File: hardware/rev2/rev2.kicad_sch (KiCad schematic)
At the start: 2 parts, among them J1 Conn_Coaxial_Small

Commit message: did some schematic stuff
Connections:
- net SX1262/Antenna: now reaches J1.1 (In)
- net GND: now reaches J1.2 (Ext)
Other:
- sheet SX1262 ports: added Antenna, BUSY, CS, DIO1, MISO, MOSI, Reset, SCK; removed none
- note added: "Cursed ribbonkabelantenn"
- moved on the sheet: J1

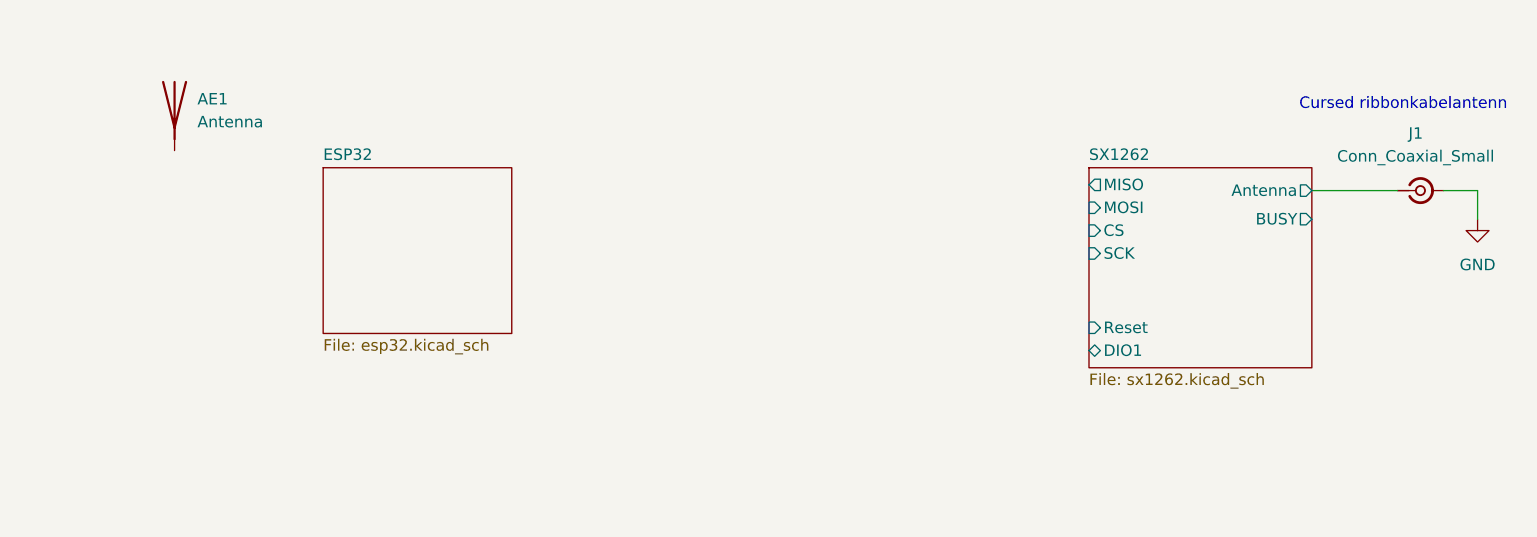
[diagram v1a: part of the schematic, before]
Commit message: wired SPI pins for SX1262
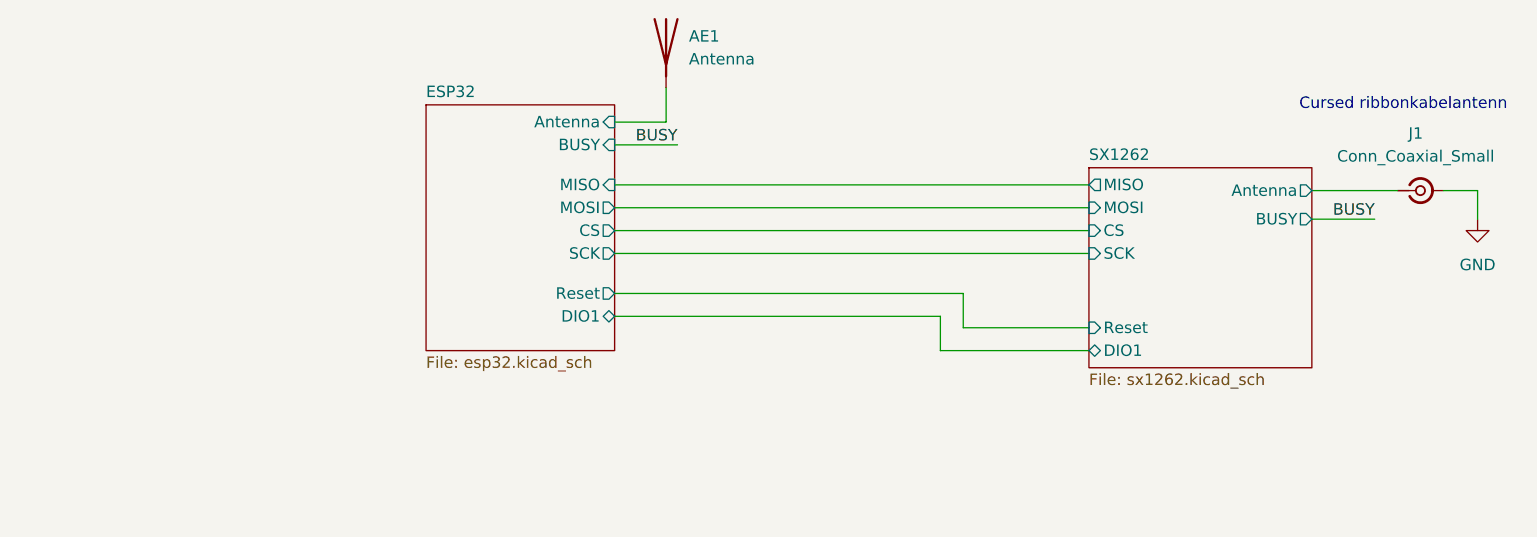
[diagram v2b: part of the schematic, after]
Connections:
- net ESP32/Antenna: now reaches AE1.1 (A)
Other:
- sheet ESP32 ports: added Antenna, BUSY, CS, DIO1, MISO, MOSI, Reset, SCK; removed none
- moved on the sheet: AE1
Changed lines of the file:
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@@
+	(wire
+		(pts
+			(xy 153.67 79.375) (xy 137.16 79.375)
+		)
+		(stroke
+			(width 0)
+			(type default)
+		)
+	)
+	(wire
+		(pts
+			(xy 100.965 68.58) (xy 153.67 68.58)
+		)
+		(stroke
+			(width 0)
+			(type default)
+		)
+	)
+	(wire
+		(pts
+			(xy 139.7 73.025) (xy 139.7 76.835)
+		)
+		(stroke
+			(width 0)
+			(type default)
+		)
+	)
+	(wire
+		(pts
+			(xy 100.965 60.96) (xy 153.67 60.96)
+		)
+		(stroke
+			(width 0)
+			(type default)
+		)
+	)
+	(wire
+		(pts
+			(xy 106.68 53.975) (xy 106.68 50.165)
+		)
+		(stroke
+			(width 0)
+			(type default)
+		)
+	)
 	(wire
 		(pts
@@
 	(wire
 		(pts
+			(xy 137.16 75.565) (xy 100.965 75.565)
+		)
+		(stroke
+			(width 0)
+			(type default)
+		)
+	)
+	(wire
+		(pts
 			(xy 178.435 61.595) (xy 187.96 61.595)
 		)
@@
 	(wire
 		(pts
+			(xy 100.965 63.5) (xy 153.67 63.5)
+		)
+		(stroke
+			(width 0)
+			(type default)
+		)
+	)
+	(wire
+		(pts
+			(xy 100.965 53.975) (xy 106.68 53.975)
+		)
+		(stroke
+			(width 0)
+			(type default)
+		)
+	)
+	(wire
+		(pts
+			(xy 185.42 64.77) (xy 178.435 64.77)
+		)
+		(stroke
+			(width 0)
+			(type default)
+		)
+	)
+	(wire
+		(pts
+			(xy 100.965 73.025) (xy 139.7 73.025)
+		)
+		(stroke
+			(width 0)
+			(type default)
+		)
+	)
+	(wire
+		(pts
 			(xy 196.85 64.77) (xy 196.85 61.595)
 		)
@@
 			(width 0)
 			(type default)
+		)
+	)
+	(wire
+		(pts
+			(xy 100.965 66.04) (xy 153.67 66.04)
+		)
+		(stroke
+			(width 0)
+			(type default)
+		)
+	)
+	(wire
+		(pts
+			(xy 137.16 79.375) (xy 137.16 75.565)
+		)
+		(stroke
+			(width 0)
+			(type default)
+		)
+	)
+	(wire
+		(pts
+			(xy 139.7 76.835) (xy 153.67 76.835)
+		)
+		(stroke
+			(width 0)
+			(type default)
+		)
+	)
+	(wire
+		(pts
+			(xy 107.95 56.515) (xy 100.965 56.515)
+		)
+		(stroke
+			(width 0)
+			(type default)
+		)
+	)
+	(label "BUSY"
+		(at 185.42 64.77 180)
+		(effects
+			(font
+				(size 1.27 1.27)
+			)
+			(justify right bottom)
+		)
+	)
+	(label "BUSY"
+		(at 107.95 56.515 180)
+		(effects
+			(font
+				(size 1.27 1.27)
+			)
+			(justify right bottom)
 		)
 	)
 	(symbol
 		(lib_id "Device:Antenna")
-		(at 52.07 52.07 0)
+		(at 106.68 45.085 0)
 		(unit 1)
 		(body_style 1)
@@
 		(fields_autoplaced yes)
 		(property "Reference" "AE1"
-			(at 54.61 51.4349 0)
+			(at 109.22 44.4499 0)
 			(show_name no)
 			(do_not_autoplace no)
@@
 		)
 		(property "Value" "Antenna"
-			(at 54.61 53.9749 0)
+			(at 109.22 46.9899 0)
 			(show_name no)
 			(do_not_autoplace no)
@@
 		)
 		(property "Footprint" ""
-			(at 52.07 52.07 0)
+			(at 106.68 45.085 0)
 			(hide yes)
 			(show_name no)
@@
 		)
 		(property "Datasheet" ""
-			(at 52.07 52.07 0)
+			(at 106.68 45.085 0)
 			(hide yes)
 			(show_name no)
@@
 		)
 		(property "Description" "Antenna"
-			(at 52.07 52.07 0)
+			(at 106.68 45.085 0)
 			(hide yes)
 			(show_name no)
@@
 	)
 	(sheet
-		(at 68.58 59.055)
-		(size 20.955 18.415)
+		(at 80.01 52.07)
+		(size 20.955 27.305)
 		(exclude_from_sim no)
 		(in_bom yes)
@@
 		)
 		(property "Sheetname" "ESP32"
-			(at 68.58 58.3434 0)
+			(at 80.01 51.3584 0)
 			(show_name no)
 			(do_not_autoplace no)
@@
 		)
 		(property "Sheetfile" "esp32.kicad_sch"
-			(at 68.58 78.0546 0)
+			(at 80.01 79.9596 0)
 			(show_name no)
 			(do_not_autoplace no)
@@
 			)
 		)
+		(pin "Antenna" input
+			(at 100.965 53.975 0)
+			(effects
+				(font
+					(size 1.27 1.27)
+				)
+				(justify right)
+			)
+		)
+		(pin "BUSY" input
+			(at 100.965 56.515 0)
+			(effects
+				(font
+					(size 1.27 1.27)
+				)
+				(justify right)
+			)
+		)
+		(pin "CS" output
+			(at 100.965 66.04 0)
+			(effects
+				(font
+					(size 1.27 1.27)
+				)
+				(justify right)
+			)
+		)
+		(pin "DIO1" bidirectional
+			(at 100.965 75.565 0)
+			(effects
+				(font
+					(size 1.27 1.27)
+				)
+				(justify right)
+			)
+		)
+		(pin "MISO" input
+			(at 100.965 60.96 0)
+			(effects
+				(font
+					(size 1.27 1.27)
+				)
+				(justify right)
+			)
+		)
+		(pin "MOSI" output
+			(at 100.965 63.5 0)
+			(effects
+				(font
+					(size 1.27 1.27)
+				)
+				(justify right)
+			)
+		)
+		(pin "Reset" output
+			(at 100.965 73.025 0)
+			(effects
+				(font
+					(size 1.27 1.27)
+				)
+				(justify right)
+			)
+		)
+		(pin "SCK" output
+			(at 100.965 68.58 0)
+			(effects
+				(font
+					(size 1.27 1.27)
+				)
+				(justify right)
+			)
+		)

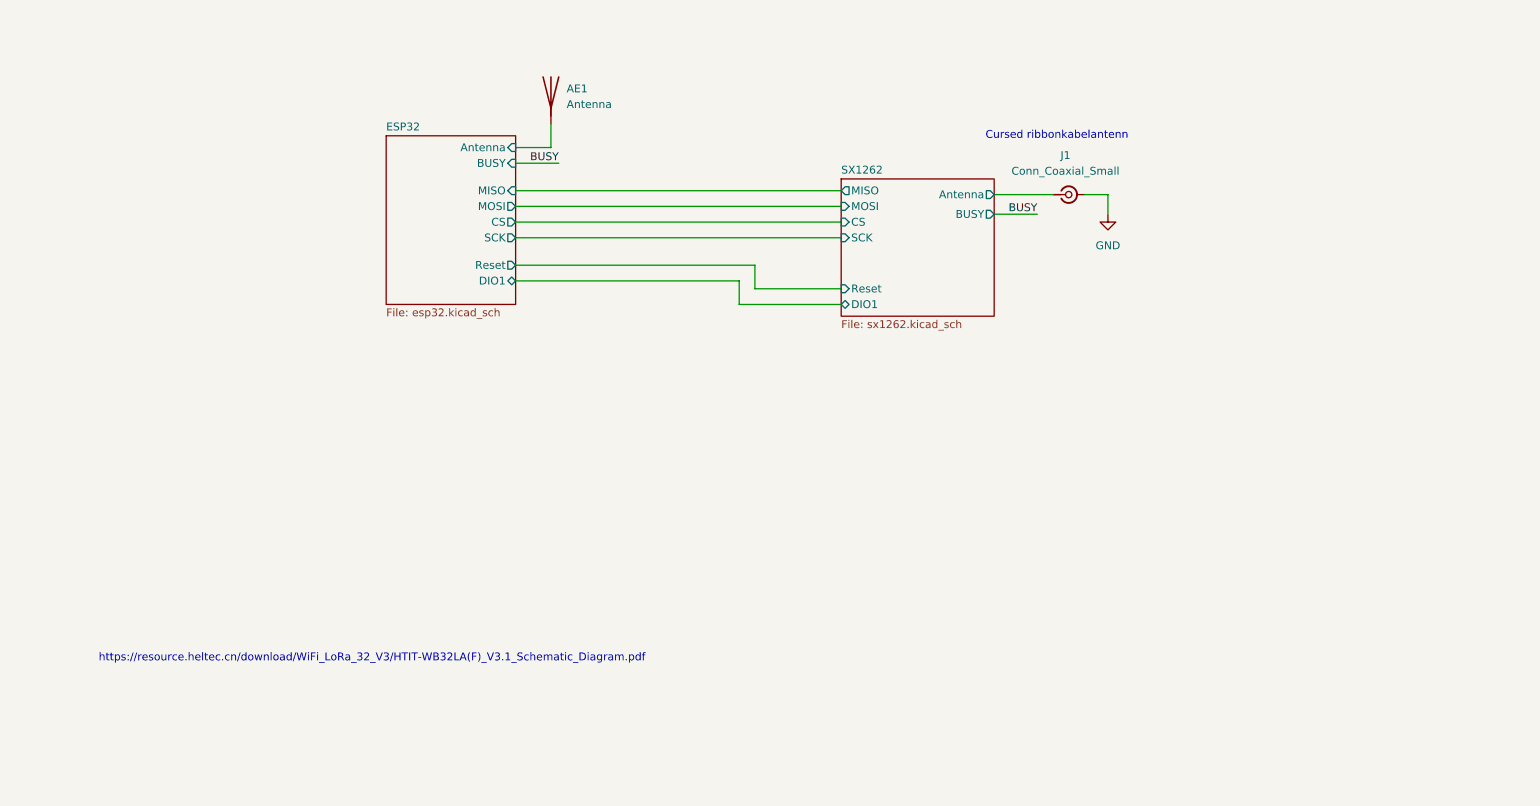
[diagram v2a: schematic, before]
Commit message: cleaned up esp32 and added antenna stuff on main sheet
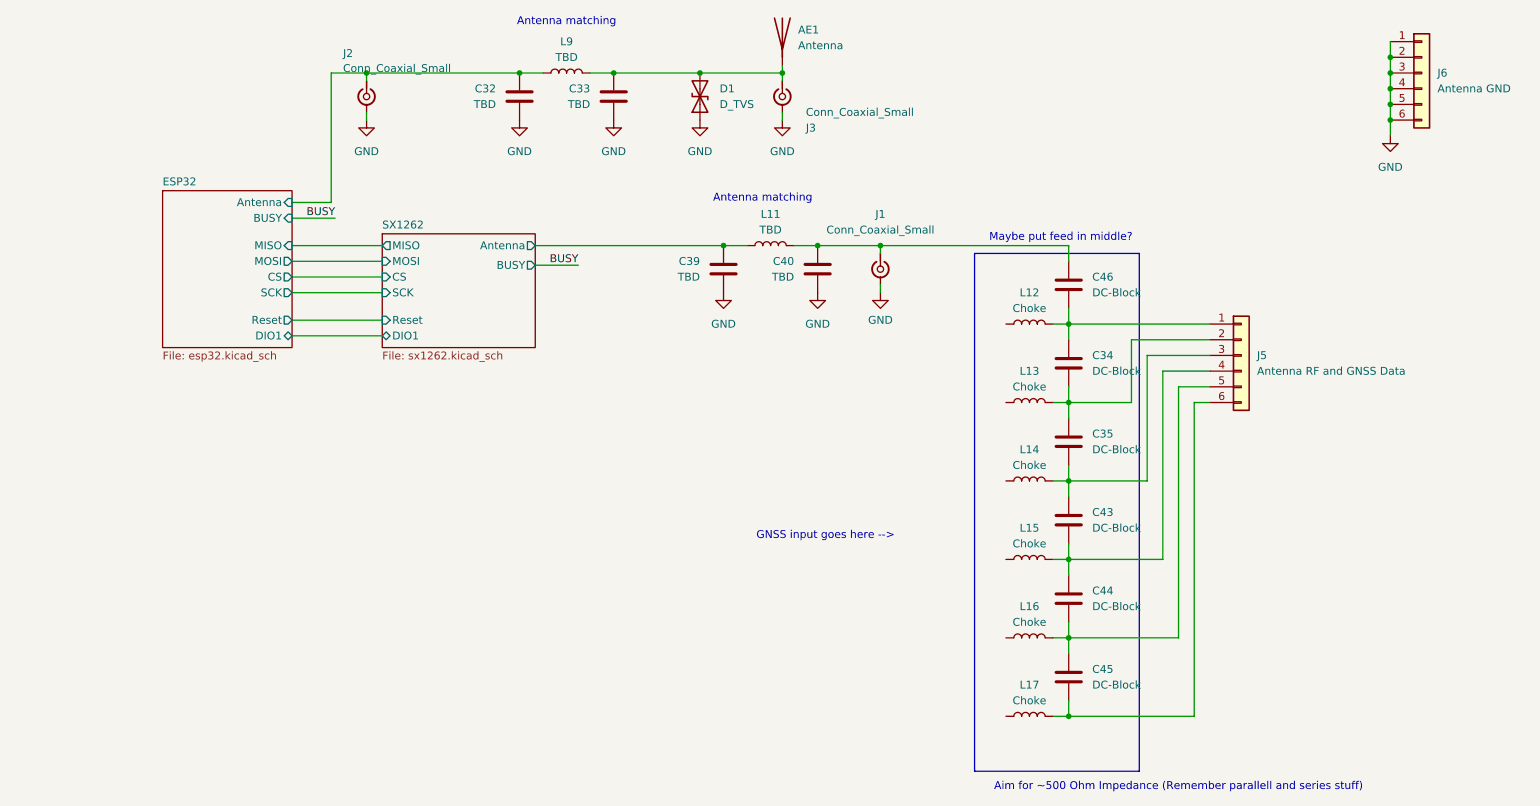
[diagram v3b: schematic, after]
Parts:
- added C32, C33, C39, C40: TBD, symbol Device:C
- added C34, C35, C43, C44, C45, C46: DC-Block, symbol Device:C
- added D1: D_TVS, symbol Device:D_TVS
- added J2, J3: Conn_Coaxial_Small, symbol Connector:Conn_Coaxial_Small
- added J5: Antenna RF and GNSS Data, symbol Connector_Generic:Conn_01x06
- added J6: Antenna GND, symbol Connector_Generic:Conn_01x06
- added L11, L9: TBD, symbol Device:L
- added L12, L13, L14, L15, L16, L17: Choke, symbol Device:L
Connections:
- net ESP32/Antenna: now also C32.1, J2.1 (In), L9.2; no longer AE1.1 (A)
- net GND: now also C32.2, C33.2, C39.2, C40.2, D1.1 (A1), J2.2 (Ext), J3.2 (Ext), J6.1 (Pin_1), J6.2 (Pin_2), J6.3 (Pin_3), J6.4 (Pin_4), J6.5 (Pin_5), J6.6 (Pin_6)
- net SX1262/Antenna: now also C39.1, L11.2; no longer J1.1 (In)
- new net: C34.2, C35.1, J5.2 (Pin_2), L13.2
- new net: C35.2, C43.1, J5.3 (Pin_3), L14.2
- new net: C43.2, C44.1, J5.4 (Pin_4), L15.2
- new net: C44.2, C45.1, J5.5 (Pin_5), L16.2
- new net: AE1.1 (A), C33.1, D1.2 (A2), J3.1 (In), L9.1
- new net: C34.1, C46.2, J5.1 (Pin_1), L12.2
- new net: C45.2, J5.6 (Pin_6), L17.2
- new net: C40.1, C46.1, J1.1 (In), L11.1
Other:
- note added: "Aim for ~500 Ohm Impedance (Remember parallell and series stuff)"
- note added: "Antenna matching"
- note added: "GNSS input goes here -->"
- note added: "Maybe put feed in middle?"
- note removed: "Cursed ribbonkabelantenn"
- note removed: "https://resource.heltec.cn/download/WiFi_LoRa_32_V3/HTIT-WB32LA(F)_V3.1_Schematic_Diagram.pdf"

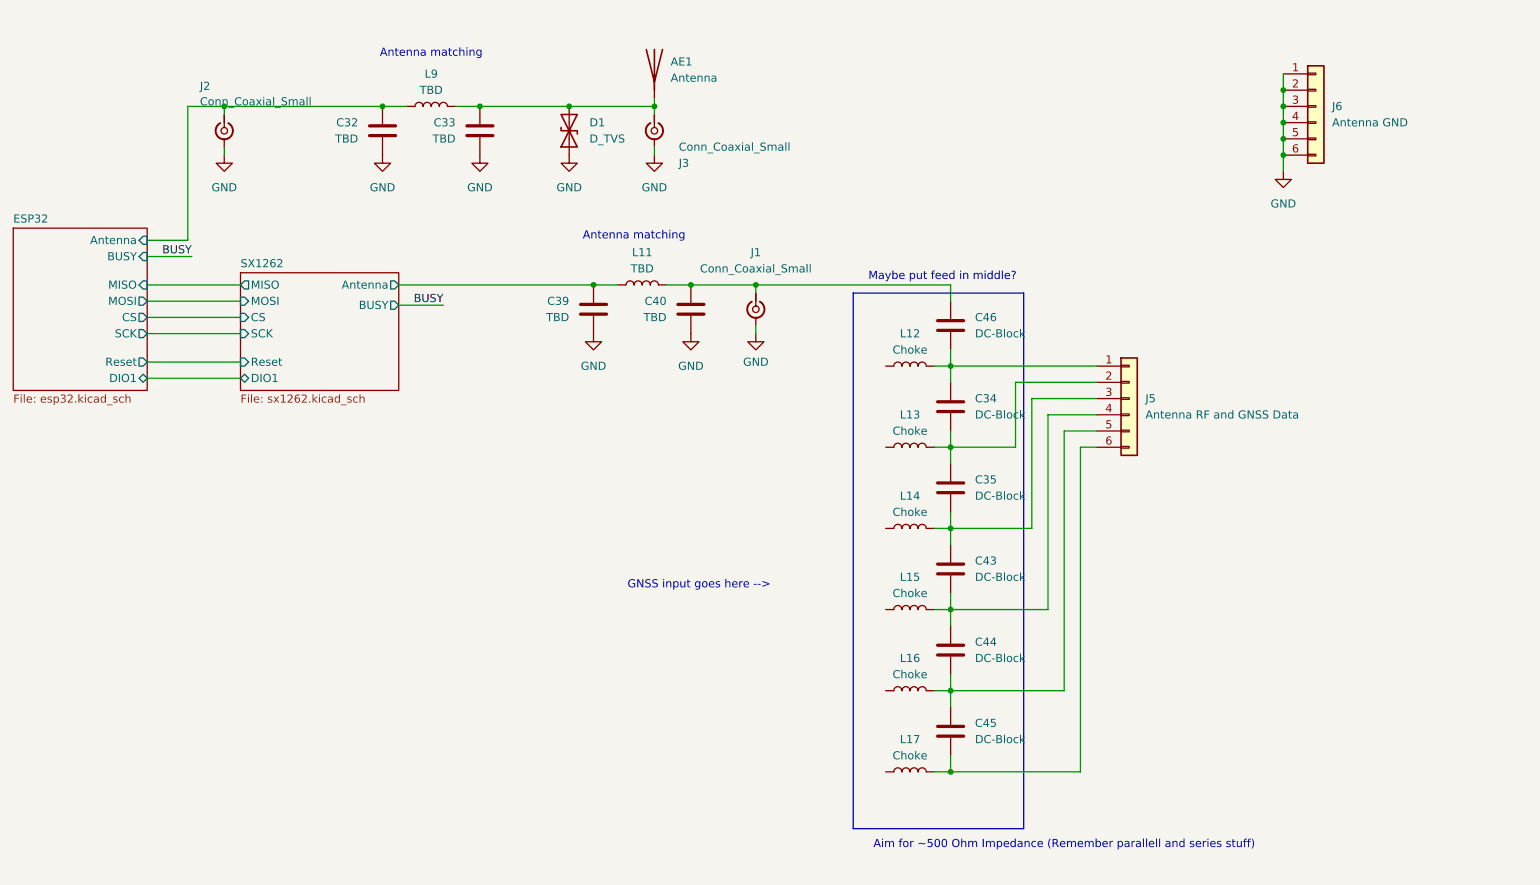
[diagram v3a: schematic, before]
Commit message: added power, net classes and some antenna stuff
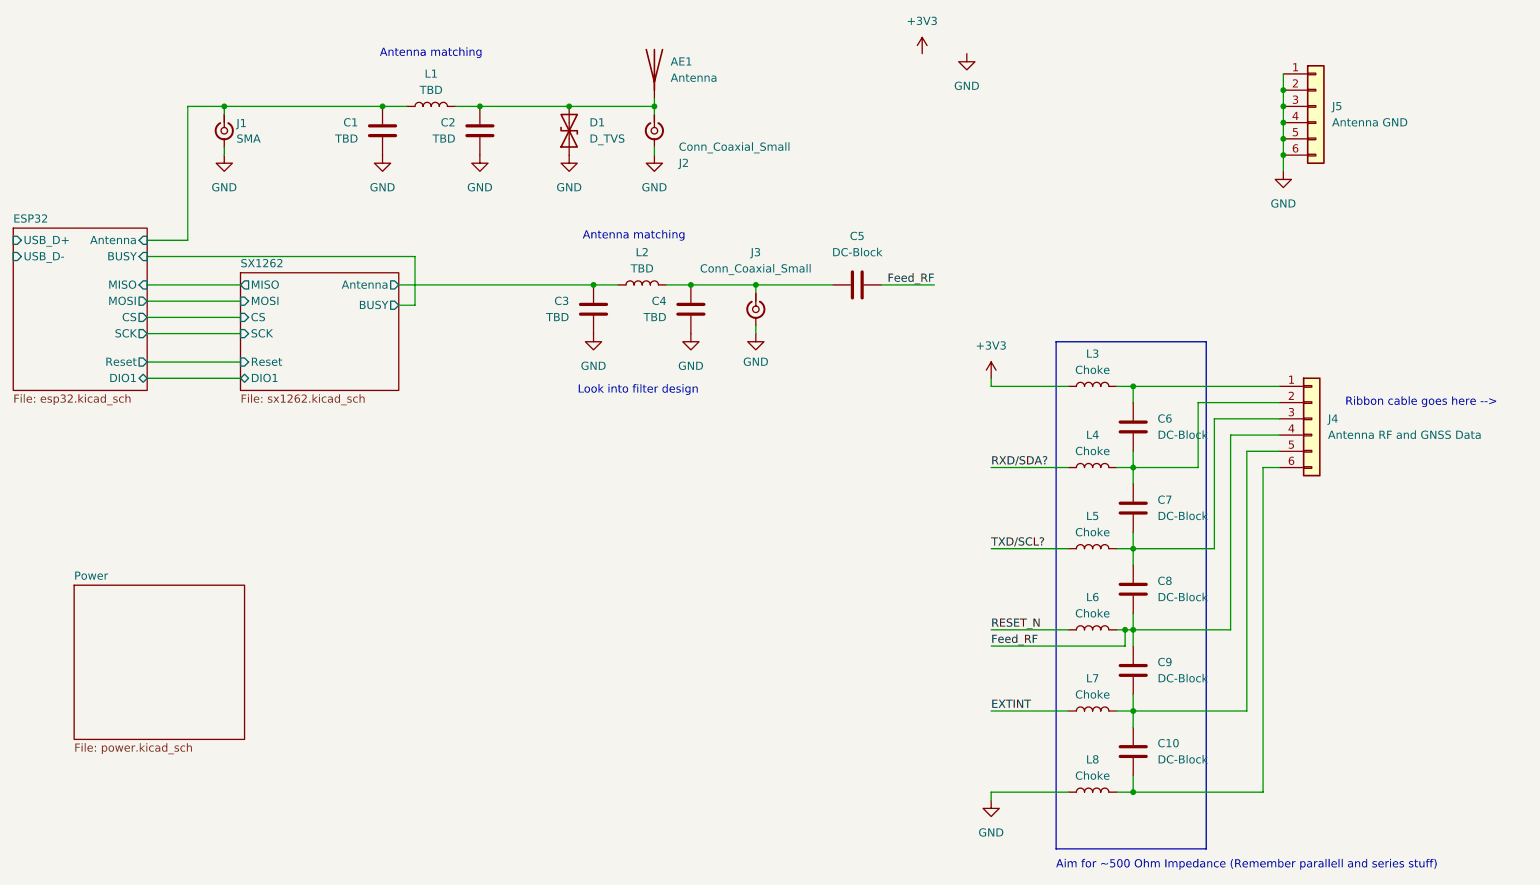
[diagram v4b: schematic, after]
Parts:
- J1: renamed from J2; value Conn_Coaxial_Small -> SMA
- renumbered C32 to C1, C45 to C10, C33 to C2, C39 to C3, C40 to C4, C46 to C5, C34 to C6, C35 to C7, C43 to C8, C44 to C9, J3 to J2, J1 to J3, J5 to J4, J6 to J5, L9 to L1, L11 to L2, L12 to L3, L13 to L4, L14 to L5, L15 to L6, L16 to L7, L17 to L8
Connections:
- net GND: now also L8.1
- net Feed_RF: now reaches C8.2, C9.1, J4.4 (Pin_4), L6.2
- net Feed_RF: now also C5.2
- net TXD/SCL?: now reaches L5.1
- net at C6.1, J4.1 (Pin_1), L3.2: no longer C5.2
- net RESET_N: now reaches L6.1
- net RXD/SDA?: now reaches L4.1
- net +3V3: now reaches L3.1
- net EXTINT: now reaches L7.1
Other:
- added sheet Power (power.kicad_sch)
- sheet ESP32 ports: added USB_D+, USB_D-; removed none
- note added: "Look into filter design"
- note added: "Ribbon cable goes here -->"
- note removed: "GNSS input goes here -->"
- note removed: "Maybe put feed in middle?"
- moved on the sheet: C10, C5, C6, C7, C8, C9, J4, L3, L4, L5, L6, L7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

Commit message: fixed some ERC errors and warnings, added USB, assigned a bunch of footprints
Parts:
- added D2, D3: D_TVS, symbol Device:D_TVS
- added J7: USB_C_Receptacle_USB2.0_16P, _footprints:SAMESKY_UJ20-C-H-G-SMT-5-P16-TR, symbol Connector:USB_C_Receptacle_USB2.0_16P
- added R10, R11: 5.1k, Inductor_SMD:L_0603_1608Metric_Pad1.05x0.95mm_HandSolder, symbol Device:R
- C1, C10, C2, C3, C4, C5, C6, C7, C8, C9: footprint (none) -> Capacitor_SMD:C_0402_1005Metric_Pad0.74x0.62mm_HandSolder
- J2, J3: value Conn_Coaxial_Small -> SMA
- L1, L2, L3, L4, L5, L6, L7, L8: footprint (none) -> Inductor_SMD:L_0402_1005Metric_Pad0.77x0.64mm_HandSolder
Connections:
- net GND: now also D2.1 (A1), D3.1 (A1), J7.A1 (GND), J7.A12 (GND), J7.B1 (GND), J7.B12 (GND), R10.2, R11.2
- net ESP32/Antenna renamed Antenna_WiFi
- net Feed_RF: no longer names the net of C5.2, C8.2, C9.1, J4.4 (Pin_4), L6.2
- net SX1262/Antenna renamed Antenna_LoRa
- new net: J7.B5 (CC2), R11.1
- new net: J7.A5 (CC1), R10.1
- new net +5V: J7.A4 (VBUS), J7.A9 (VBUS), J7.B4 (VBUS), J7.B9 (VBUS)
- new net USB_D+: D3.2 (A2), J7.A6 (D+), J7.B6 (D+)
- new net USB_D-: D2.2 (A2), J7.A7 (D-), J7.B7 (D-)
- no-connect marks 0 -> 3
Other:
- sheet SX1262 ports: added RX_EN; removed none
- note added: "Net assignments"
- note added: "USB Connection"
- note added: "WiFi Antenna"
- moved on the sheet: AE1, C1, C10, C2, C3, C4, C5, C6, C7, C8, C9, D1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
